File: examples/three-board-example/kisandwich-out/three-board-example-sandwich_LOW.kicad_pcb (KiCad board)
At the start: 6 copper layers, 55 x 55.8 mm, 1 part, among them U1 LM555xM

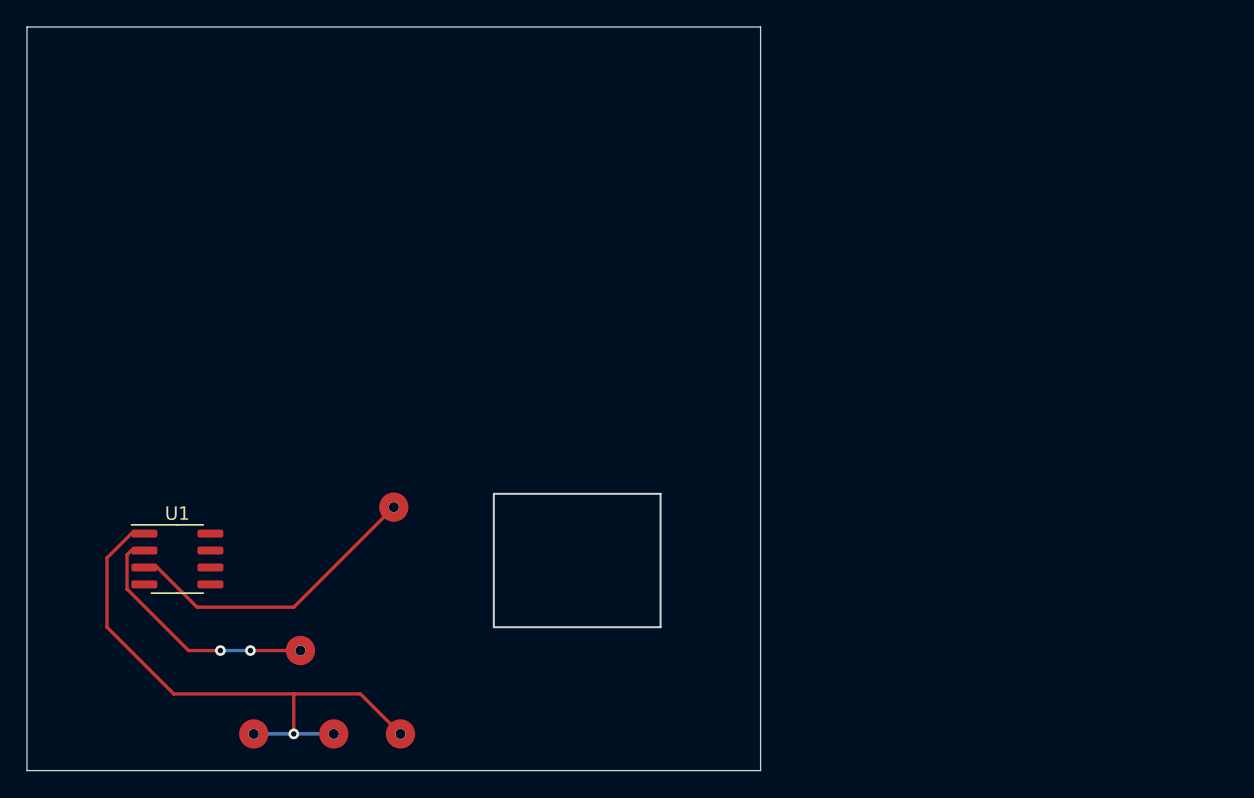
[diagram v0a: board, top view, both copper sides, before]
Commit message: Made 3D representations. Changed speaker to being placed on midboard. Checked heights
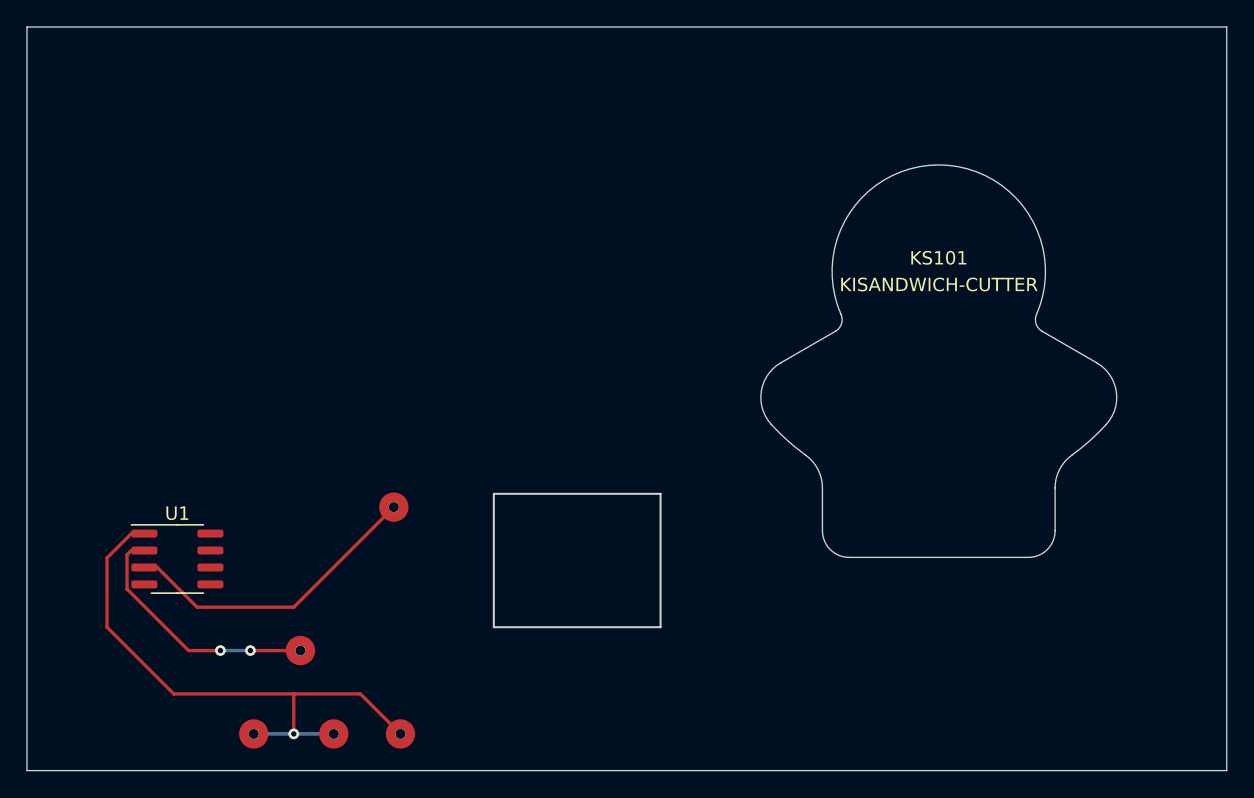
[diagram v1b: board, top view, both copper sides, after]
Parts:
- added KS101: KISANDWICH-CUTTER, Alex_Connectors:CUI-speaker-3layer-tight, F.Cu at (213.4, 53.3)
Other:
- board size 55 x 55.8 mm -> 89.9 x 55.8 mm
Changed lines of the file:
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@@
     (tracks 28)
     (zones 0)
-    (modules 1)
+    (modules 2)
     (nets 9)
   )
@@
     (add_net "Net-(U1-Pad8)")
   )
+  (module Alex_Connectors:CUI-speaker-3layer-tight (layer F.Cu)
+    (at 213.36 53.34 180)
+    (descr "STD_v2_allSketches StepUp generated footprint")
+    (attr smd)
+    (fp_text reference KS101 (at 0 1) (layer F.SilkS)
+      (effects (font (size 1 1) (thickness 0.15)))
+    )
+    (fp_text value KISANDWICH-CUTTER (at 0 -1) (layer F.SilkS)
+      (effects (font (size 1 1) (thickness 0.15)))
+    )
+    (fp_line (start -6.723 -21.425) (end 6.723 -21.425) (layer Edge.Cuts) (width 0.1))
+    (fp_line (start 8.723 -16.204) (end 8.723 -19.425) (layer Edge.Cuts) (width 0.1))
+    (fp_line (start -8.723 -16.204) (end -8.723 -19.425) (layer Edge.Cuts) (width 0.1))
+    (fp_line (start 7.746 -4.472) (end 11.843 -6.837) (layer Edge.Cuts) (width 0.1))
+    (fp_line (start -7.746 -4.472) (end -11.843 -6.837) (layer Edge.Cuts) (width 0.1))
+    (fp_text user %R (at 0 1) (layer F.Fab)
+      (effects (font (size 1 1) (thickness 0.15)))
+    )
+    (fp_text user "EDIT PAD NUMBERS" (at 0 -2) (layer Cmts.User)
+      (effects (font (size 1 1) (thickness 0.2) italic))
+    )
+    (fp_arc (start 0 0) (end -7.33 -3.205) (angle -227.241) (layer Edge.Cuts) (width 0.1))
+    (fp_arc (start 0 0) (end 12.559 -11.457) (angle -11.743) (layer Edge.Cuts) (width 0.1))
+    (fp_arc (start -10.343 -9.435) (end -12.559 -11.457) (angle -102.374) (layer Edge.Cuts) (width 0.1))
+    (fp_arc (start -8.246 -3.606) (end -7.33 -3.205) (angle -83.621) (layer Edge.Cuts) (width 0.1))
+    (fp_arc (start 8.246 -3.606) (end 7.746 -4.472) (angle -83.621) (layer Edge.Cuts) (width 0.1))
+    (fp_arc (start 10.343 -9.435) (end 11.843 -6.837) (angle -102.374) (layer Edge.Cuts) (width 0.1))
+    (fp_arc (start -6.723 -19.425) (end -6.723 -21.425) (angle -90) (layer Edge.Cuts) (width 0.1))
+    (fp_arc (start 6.723 -19.425) (end 8.723 -19.425) (angle -90) (layer Edge.Cuts) (width 0.1))
+    (fp_arc (start 0 0) (end -9.964 -13.774) (angle -11.743) (layer Edge.Cuts) (width 0.1))
+    (fp_arc (start -11.723 -16.204) (end -9.964 -13.774) (angle -54.117) (layer Edge.Cuts) (width 0.1))
+    (fp_arc (start 11.723 -16.204) (end 8.723 -16.204) (angle -54.117) (layer Edge.Cuts) (width 0.1))
+  )
   (module Package_SO:SOIC-8_3.9x4.9mm_P1.27mm (layer F.Cu)
     (at 156.275 74.885)
@@
   (gr_line (start 192.5 70) (end 180 70) (layer Edge.Cuts) (width 0.15))
   (gr_line (start 145 90.75) (end 145 35) (layer Edge.Cuts) (width 0.05))
-  (gr_line (start 200 90.75) (end 145 90.75) (layer Edge.Cuts) (width 0.05))
-  (gr_line (start 200 35) (end 200 90.75) (layer Edge.Cuts) (width 0.05))
-  (gr_line (start 145 35) (end 200 35) (layer Edge.Cuts) (width 0.05))
+  (gr_line (start 234.95 90.75) (end 145 90.75) (layer Edge.Cuts) (width 0.05))
+  (gr_line (start 234.95 35) (end 234.95 90.75) (layer Edge.Cuts) (width 0.05))
+  (gr_line (start 145 35) (end 234.95 35) (layer Edge.Cuts) (width 0.05))
   (segment (start 153.8 75.52) (end 154.77 75.52) (width 0.25) (layer F.Cu) (net 6))
   (segment (start 154.77 75.52) (end 157.75 78.5) (width 0.25) (layer F.Cu) (net 6))

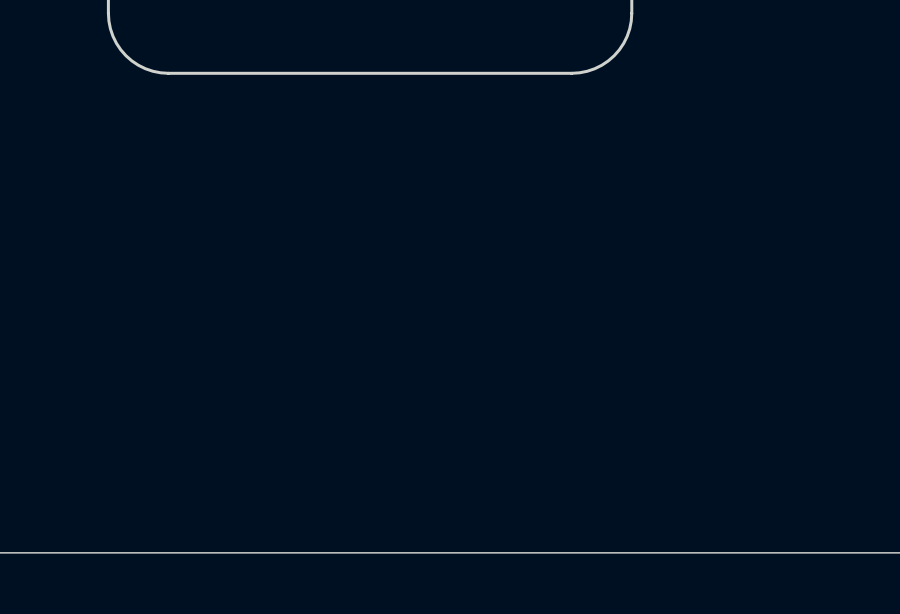
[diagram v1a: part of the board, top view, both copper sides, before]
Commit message: Also processing copper that is in cutter modules
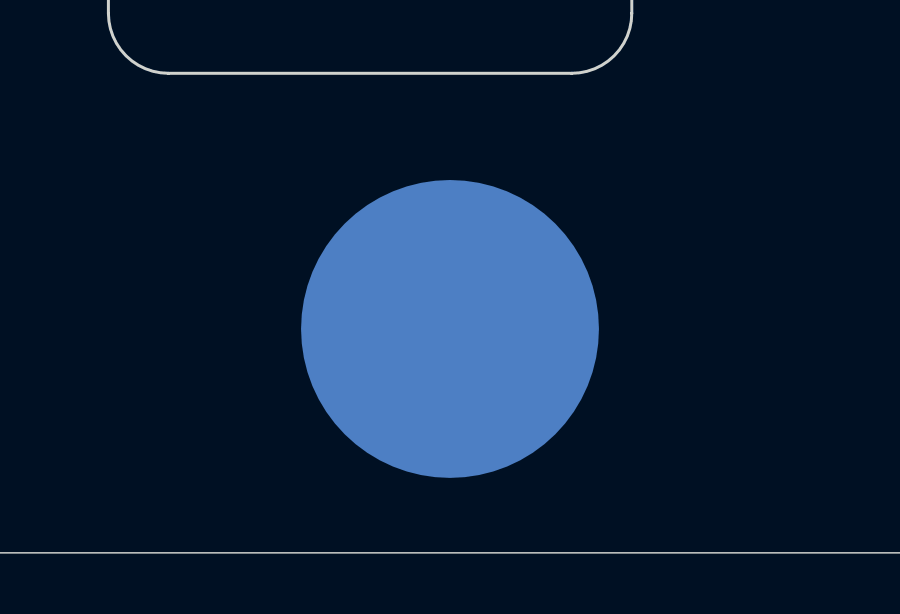
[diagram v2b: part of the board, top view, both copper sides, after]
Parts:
- added svg2mod: KISANDWICH-CUTTER, Alex_Sandwiches:light-hole, F.Cu at (201.9, 77.5)
